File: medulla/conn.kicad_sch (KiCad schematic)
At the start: 7 parts

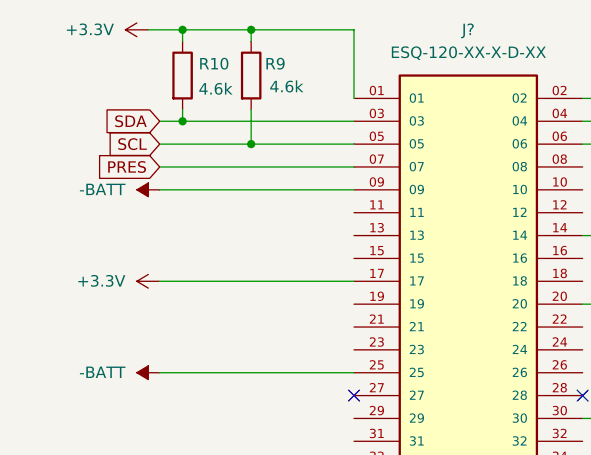
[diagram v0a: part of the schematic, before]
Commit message: alpha 0.2.0: Added RP2040, LM2936-3.3V Regulator, removed ADS1115, PCA9685
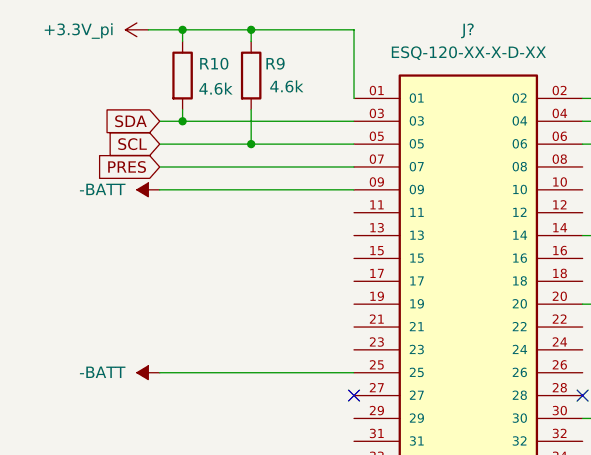
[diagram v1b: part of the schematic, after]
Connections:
- net +3.3V renamed +3.3V_pi
- net +3.3V_pi: no longer J?.17
